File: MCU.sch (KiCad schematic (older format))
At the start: 10 parts

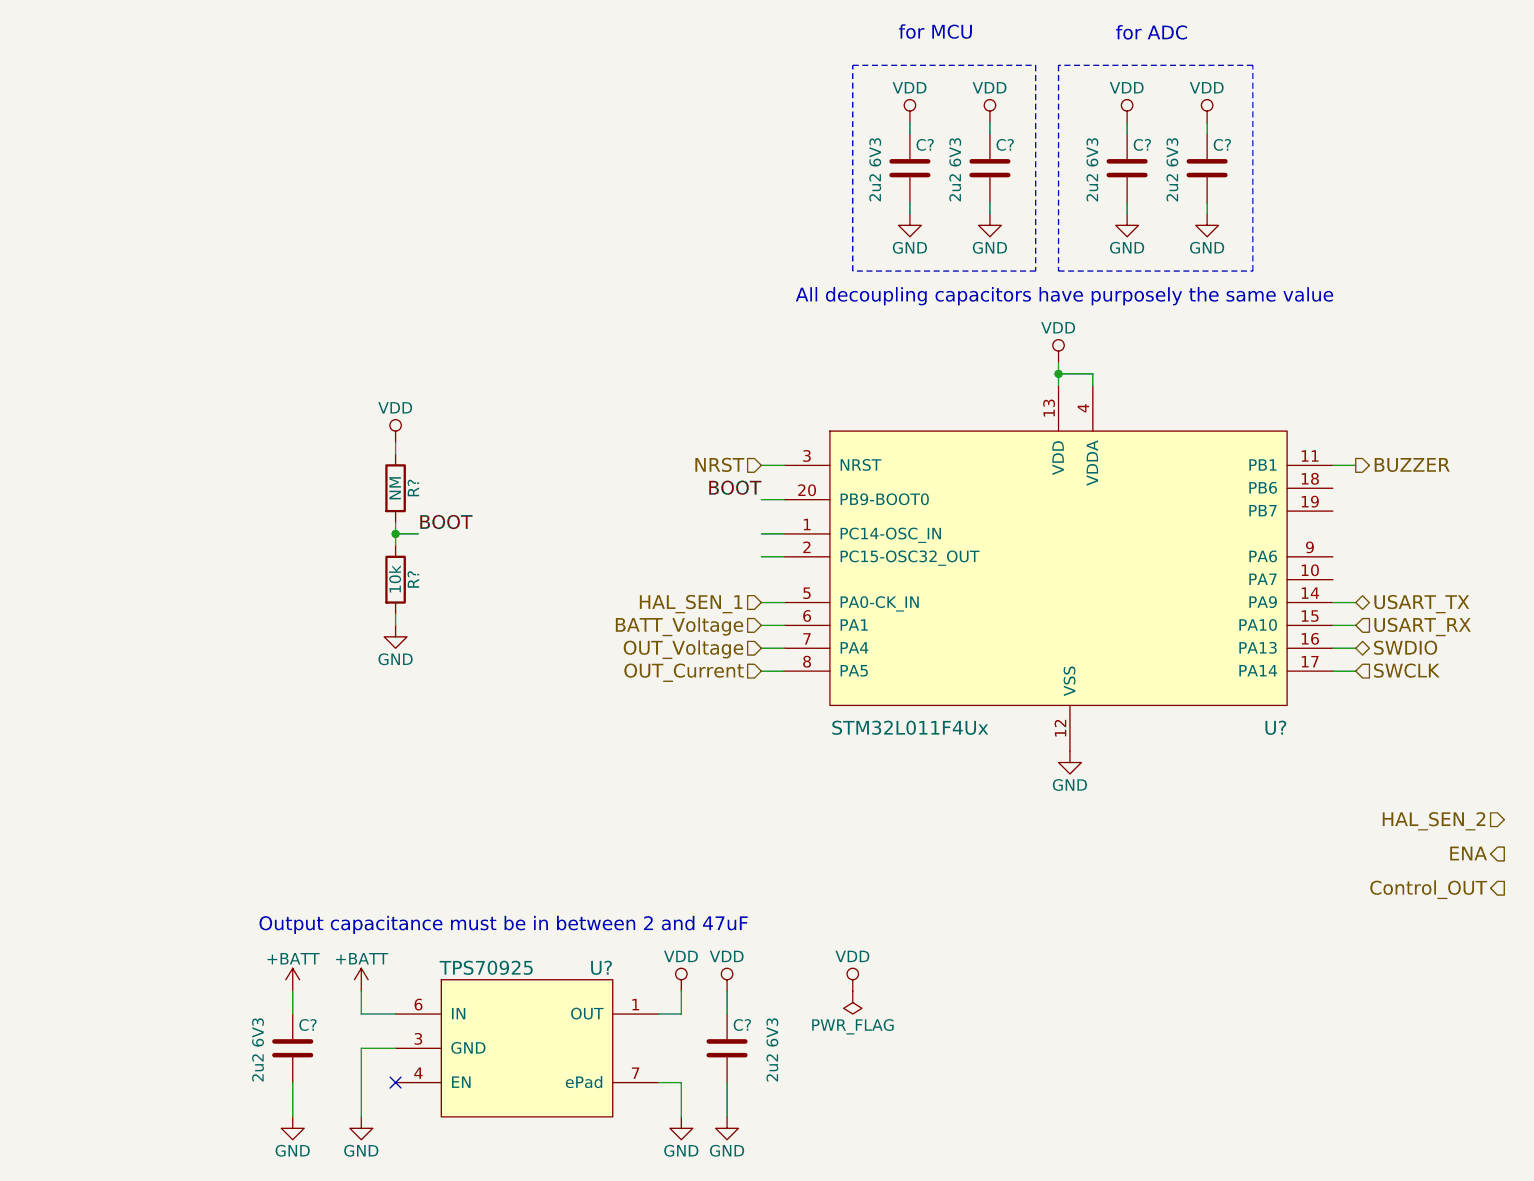
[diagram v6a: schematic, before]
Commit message: added few MPNs
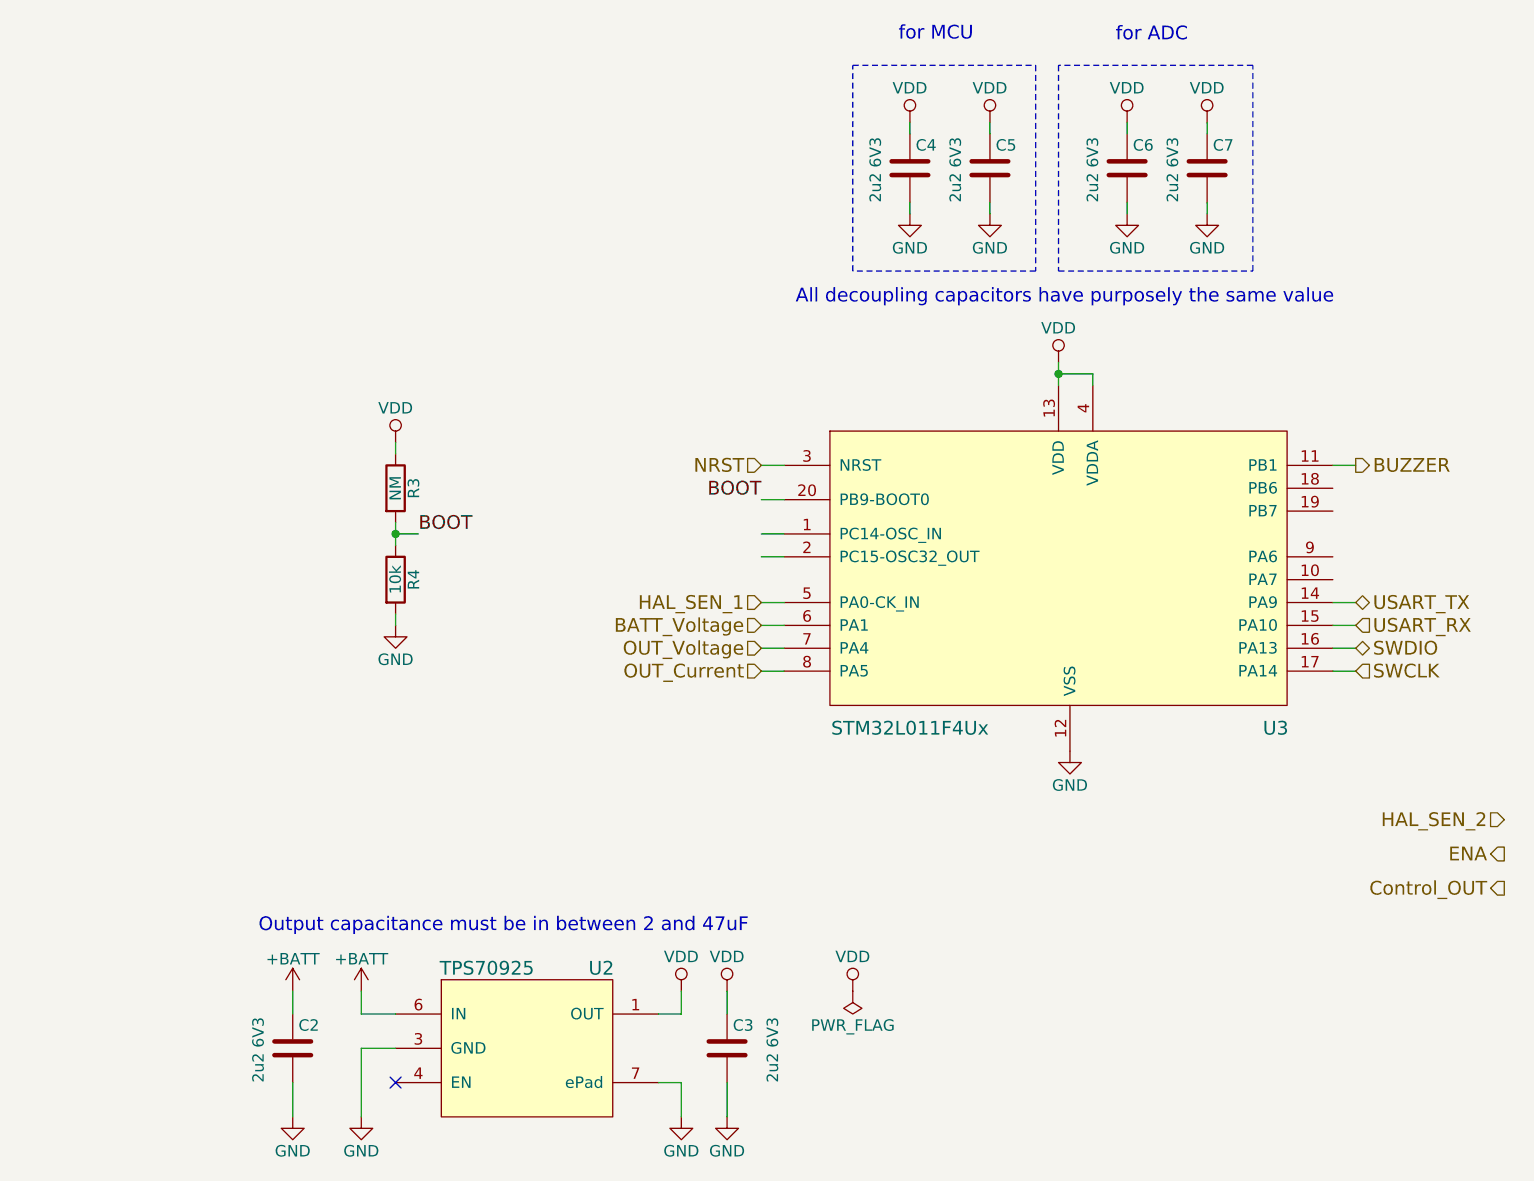
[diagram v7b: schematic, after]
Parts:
- gave numbers to parts that had none: 10
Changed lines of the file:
@@
 $EndDescr
 $Comp
-L VDD #PWR?
+L VDD #PWR30
 U 1 1 5A9B30A9
 P 6100 3250
-F 0 "#PWR?" H 6100 3100 50  0001 C CNN
+F 0 "#PWR30" H 6100 3100 50  0001 C CNN
 F 1 "VDD" H 6100 3400 50  0000 C CNN
 F 2 "" H 6100 3250 50  0001 C CNN
@@
 Connection ~ 6100 3300
 $Comp
-L GND #PWR?
+L GND #PWR31
 U 1 1 5A9B30B3
 P 6150 4950
-F 0 "#PWR?" H 6150 4700 50  0001 C CNN
+F 0 "#PWR31" H 6150 4700 50  0001 C CNN
 F 1 "GND" H 6150 4800 50  0000 C CNN
 F 2 "" H 6150 4950 50  0001 C CNN
@@
 $EndComp
 $Comp
-L GND #PWR?
+L GND #PWR18
 U 1 1 5A9B3148
 P 3050 6550
-F 0 "#PWR?" H 3050 6300 50  0001 C CNN
+F 0 "#PWR18" H 3050 6300 50  0001 C CNN
 F 1 "GND" H 3050 6400 50  0000 C CNN
 F 2 "" H 3050 6550 50  0001 C CNN
@@
 NoConn ~ 3200 6400
 $Comp
-L GND #PWR?
+L GND #PWR22
 U 1 1 5A9B3188
 P 4450 6550
-F 0 "#PWR?" H 4450 6300 50  0001 C CNN
+F 0 "#PWR22" H 4450 6300 50  0001 C CNN
 F 1 "GND" H 4450 6400 50  0000 C CNN
 F 2 "" H 4450 6550 50  0001 C CNN
@@
 	4450 6400 4450 6550
 $Comp
-L VDD #PWR?
+L VDD #PWR21
 U 1 1 5A9B31B3
 P 4450 6000
-F 0 "#PWR?" H 4450 5850 50  0001 C CNN
+F 0 "#PWR21" H 4450 5850 50  0001 C CNN
 F 1 "VDD" H 4450 6150 50  0000 C CNN
 F 2 "" H 4450 6000 50  0001 C CNN
@@
 	4450 6100 4350 6100
 $Comp
-L +BATT #PWR?
+L +BATT #PWR17
 U 1 1 5A9B31F8
 P 3050 6000
-F 0 "#PWR?" H 3050 5850 50  0001 C CNN
+F 0 "#PWR17" H 3050 5850 50  0001 C CNN
 F 1 "+BATT" H 3050 6140 50  0000 C CNN
 F 2 "" H 3050 6000 50  0001 C CNN
@@
 	3050 6100 3200 6100
 $Comp
-L C C?
+L C C3
 U 1 1 5A9B323D
 P 4650 6250
-F 0 "C?" H 4675 6350 50  0000 L CNN
+F 0 "C3" H 4675 6350 50  0000 L CNN
 F 1 "2u2 6V3" V 4850 6100 50  0000 L CNN
 F 2 "" H 4688 6100 50  0001 C CNN
@@
 $EndComp
 $Comp
-L VDD #PWR?
+L VDD #PWR23
 U 1 1 5A9B32A8
 P 4650 6000
-F 0 "#PWR?" H 4650 5850 50  0001 C CNN
+F 0 "#PWR23" H 4650 5850 50  0001 C CNN
 F 1 "VDD" H 4650 6150 50  0000 C CNN
 F 2 "" H 4650 6000 50  0001 C CNN
@@
 $EndComp
 $Comp
-L GND #PWR?
+L GND #PWR24
 U 1 1 5A9B32D5
 P 4650 6550
-F 0 "#PWR?" H 4650 6300 50  0001 C CNN
+F 0 "#PWR24" H 4650 6300 50  0001 C CNN
 F 1 "GND" H 4650 6400 50  0000 C CNN
 F 2 "" H 4650 6550 50  0001 C CNN
@@
 	4650 6400 4650 6550
 $Comp
-L C C?
+L C C2
 U 1 1 5A9B33BC
 P 2750 6250
-F 0 "C?" H 2775 6350 50  0000 L CNN
+F 0 "C2" H 2775 6350 50  0000 L CNN
 F 1 "2u2 6V3" V 2600 6100 50  0000 L CNN
 F 2 "" H 2788 6100 50  0001 C CNN
@@
 $EndComp
 $Comp
-L GND #PWR?
+L GND #PWR16
 U 1 1 5A9B33C8
 P 2750 6550
-F 0 "#PWR?" H 2750 6300 50  0001 C CNN
+F 0 "#PWR16" H 2750 6300 50  0001 C CNN
 F 1 "GND" H 2750 6400 50  0000 C CNN
 F 2 "" H 2750 6550 50  0001 C CNN
@@
 	2750 6400 2750 6550
 $Comp
-L +BATT #PWR?
+L +BATT #PWR15
 U 1 1 5A9B33E9
 P 2750 6000
-F 0 "#PWR?" H 2750 5850 50  0001 C CNN
+F 0 "#PWR15" H 2750 5850 50  0001 C CNN
 F 1 "+BATT" H 2750 6140 50  0000 C CNN
 F 2 "" H 2750 6000 50  0001 C CNN
@@
 $EndComp
 $Comp
-L C C?
+L C C4
 U 1 1 5A9B3893
 P 5450 2400
-F 0 "C?" H 5475 2500 50  0000 L CNN
+F 0 "C4" H 5475 2500 50  0000 L CNN
 F 1 "2u2 6V3" V 5300 2250 50  0000 L CNN
 F 2 "" H 5488 2250 50  0001 C CNN
@@
 Output capacitance must be in between 2 and 47uF\n
 $Comp
-L VDD #PWR?
+L VDD #PWR26
 U 1 1 5A9B3944
 P 5450 2200
-F 0 "#PWR?" H 5450 2050 50  0001 C CNN
+F 0 "#PWR26" H 5450 2050 50  0001 C CNN
 F 1 "VDD" H 5450 2350 50  0000 C CNN
 F 2 "" H 5450 2200 50  0001 C CNN
@@
 	5450 2200 5450 2250
 $Comp
-L GND #PWR?
+L GND #PWR27
 U 1 1 5A9B3984
 P 5450 2600
-F 0 "#PWR?" H 5450 2350 50  0001 C CNN
+F 0 "#PWR27" H 5450 2350 50  0001 C CNN
 F 1 "GND" H 5450 2450 50  0000 C CNN
 F 2 "" H 5450 2600 50  0001 C CNN
@@
 	5450 2550 5450 2600
 $Comp
-L C C?
+L C C5
 U 1 1 5A9B39ED
 P 5800 2400
-F 0 "C?" H 5825 2500 50  0000 L CNN
+F 0 "C5" H 5825 2500 50  0000 L CNN
 F 1 "2u2 6V3" V 5650 2250 50  0000 L CNN
 F 2 "" H 5838 2250 50  0001 C CNN
@@
 $EndComp
 $Comp
-L VDD #PWR?
+L VDD #PWR28
 U 1 1 5A9B39F3
 P 5800 2200
-F 0 "#PWR?" H 5800 2050 50  0001 C CNN
+F 0 "#PWR28" H 5800 2050 50  0001 C CNN
 F 1 "VDD" H 5800 2350 50  0000 C CNN
 F 2 "" H 5800 2200 50  0001 C CNN
@@
 	5800 2200 5800 2250
 $Comp
-L GND #PWR?
+L GND #PWR29
 U 1 1 5A9B39FA
 P 5800 2600
-F 0 "#PWR?" H 5800 2350 50  0001 C CNN
+F 0 "#PWR29" H 5800 2350 50  0001 C CNN
 F 1 "GND" H 5800 2450 50  0000 C CNN
 F 2 "" H 5800 2600 50  0001 C CNN
@@
 	5800 2550 5800 2600
 $Comp
-L C C?
+L C C6
 U 1 1 5A9B3B25
 P 6400 2400
-F 0 "C?" H 6425 2500 50  0000 L CNN
+F 0 "C6" H 6425 2500 50  0000 L CNN
 F 1 "2u2 6V3" V 6250 2250 50  0000 L CNN
 F 2 "" H 6438 2250 50  0001 C CNN
@@
 $EndComp
 $Comp
-L VDD #PWR?
+L VDD #PWR32
 U 1 1 5A9B3B2B
 P 6400 2200
-F 0 "#PWR?" H 6400 2050 50  0001 C CNN
+F 0 "#PWR32" H 6400 2050 50  0001 C CNN
 F 1 "VDD" H 6400 2350 50  0000 C CNN
 F 2 "" H 6400 2200 50  0001 C CNN
@@
 	6400 2200 6400 2250
 $Comp
-L GND #PWR?
+L GND #PWR33
 U 1 1 5A9B3B32
 P 6400 2600
-F 0 "#PWR?" H 6400 2350 50  0001 C CNN
+F 0 "#PWR33" H 6400 2350 50  0001 C CNN
 F 1 "GND" H 6400 2450 50  0000 C CNN
 F 2 "" H 6400 2600 50  0001 C CNN
@@
 	6400 2550 6400 2600
 $Comp
-L C C?
+L C C7
 U 1 1 5A9B3B84
 P 6750 2400
-F 0 "C?" H 6775 2500 50  0000 L CNN
+F 0 "C7" H 6775 2500 50  0000 L CNN
 F 1 "2u2 6V3" V 6600 2250 50  0000 L CNN
 F 2 "" H 6788 2250 50  0001 C CNN
@@
 $EndComp
 $Comp
-L VDD #PWR?
+L VDD #PWR34
 U 1 1 5A9B3B8A
 P 6750 2200
-F 0 "#PWR?" H 6750 2050 50  0001 C CNN
+F 0 "#PWR34" H 6750 2050 50  0001 C CNN
 F 1 "VDD" H 6750 2350 50  0000 C CNN
 F 2 "" H 6750 2200 50  0001 C CNN
@@
 	6750 2200 6750 2250
 $Comp
-L GND #PWR?
+L GND #PWR35
 U 1 1 5A9B3B91
 P 6750 2600
-F 0 "#PWR?" H 6750 2350 50  0001 C CNN
+F 0 "#PWR35" H 6750 2350 50  0001 C CNN
 F 1 "GND" H 6750 2450 50  0000 C CNN
 F 2 "" H 6750 2600 50  0001 C CNN
@@
 	7300 4500 7400 4500
 $Comp
-L R R?
+L R R4
 U 1 1 5A9B431F
 P 3200 4200
-F 0 "R?" V 3280 4200 50  0000 C CNN
+F 0 "R4" V 3280 4200 50  0000 C CNN
 F 1 "10k" V 3200 4200 50  0000 C CNN
 F 2 "" V 3130 4200 50  0001 C CNN
@@
 $EndComp
 $Comp
-L R R?
+L R R3
 U 1 1 5A9B4434
 P 3200 3800
-F 0 "R?" V 3280 3800 50  0000 C CNN
+F 0 "R3" V 3280 3800 50  0000 C CNN
 F 1 "NM" V 3200 3800 50  0000 C CNN
 F 2 "" V 3130 3800 50  0001 C CNN
@@
 $EndComp
 $Comp
-L VDD #PWR?
+L VDD #PWR19
 U 1 1 5A9B4476
 P 3200 3600
-F 0 "#PWR?" H 3200 3450 50  0001 C CNN
+F 0 "#PWR19" H 3200 3450 50  0001 C CNN
 F 1 "VDD" H 3200 3750 50  0000 C CNN
 F 2 "" H 3200 3600 50  0001 C CNN
@@
 	3200 3650 3200 3600
 $Comp
-L GND #PWR?
+L GND #PWR20
 U 1 1 5A9B4528
 P 3200 4400
-F 0 "#PWR?" H 3200 4150 50  0001 C CNN
+F 0 "#PWR20" H 3200 4150 50  0001 C CNN
 F 1 "GND" H 3200 4250 50  0000 C CNN
 F 2 "" H 3200 4400 50  0001 C CNN
@@
 HAL_SEN_2
 $Comp
-L PWR_FLAG #FLG?
+L PWR_FLAG #FLG3
 U 1 1 5AA0AD8D
 P 5200 6000
-F 0 "#FLG?" H 5200 6075 50  0001 C CNN
+F 0 "#FLG3" H 5200 6075 50  0001 C CNN
 F 1 "PWR_FLAG" H 5200 6150 50  0000 C CNN
 F 2 "" H 5200 6000 50  0001 C CNN
@@
 $EndComp
 $Comp
-L VDD #PWR?
+L VDD #PWR25
 U 1 1 5AA0ADBD
 P 5200 6000
-F 0 "#PWR?" H 5200 5850 50  0001 C CNN
+F 0 "#PWR25" H 5200 5850 50  0001 C CNN
 F 1 "VDD" H 5200 6150 50  0000 C CNN
 F 2 "" H 5200 6000 50  0001 C CNN
@@
 	4800 4100 4900 4100
 $Comp
-L STM32L011F4Ux U?
+L STM32L011F4Ux U3
 U 1 1 5AA7A3A1
 P 6150 4200
-F 0 "U?" H 7050 3550 60  0000 C CNN
+F 0 "U3" H 7050 3550 60  0000 C CNN
 F 1 "STM32L011F4Ux" H 5450 3550 60  0000 C CNN
 F 2 "Housings_DFN_QFN:ST_UFQFPN-20_3x3mm_Pitch0.5mm" H 6150 3300 60  0001 C CNN
@@
 $EndComp
 $Comp
-L TPS709 U?
+L TPS709 U2
 U 1 1 5AA7A66F
 P 3800 6250
-F 0 "U?" H 4100 6600 60  0000 C CNN
+F 0 "U2" H 4100 6600 60  0000 C CNN
 F 1 "TPS70925" H 3600 6600 60  0000 C CNN
 F 2 "lakotamm-miscellaneous:WSON-6_2x2mm_Pitch0.65mm" H 3850 5600 60  0001 C CNN

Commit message: Progress on the charging circuit
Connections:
- net labels added: Charge_control, Enable_boost, Voltage_control, ~CHARGING
- net labels removed: Control_OUT, ENA
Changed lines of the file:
@@
 BUZZER
 Text HLabel 8050 5550 0    60   Output ~ 0
-Control_OUT
+Voltage_control
 Text HLabel 8050 5400 0    60   Output ~ 0
-ENA
+Enable_boost
 Text HLabel 4800 4500 0    60   Input ~ 0
 OUT_Voltage
@@
 Text Notes 4950 3000 0    60   ~ 0
 All decoupling capacitors have purposely the same value\n
+Text HLabel 8050 5700 0    60   Input ~ 0
+~CHARGING
+Text HLabel 8050 5850 0    60   Output ~ 0
+Charge_control
 $EndSCHEMATC
